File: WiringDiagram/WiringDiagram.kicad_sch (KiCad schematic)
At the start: 30 parts, among them J1 Conn_01x06, J2 Conn_01x02, J3 Conn_01x04, J4 Conn_01x04, J5 Conn_01x06, J8 FTDI SERIAL, SW1 TELEMETRUM ROTARY SWITCH, SW2 ERS SENDER ROTARY SWITCH

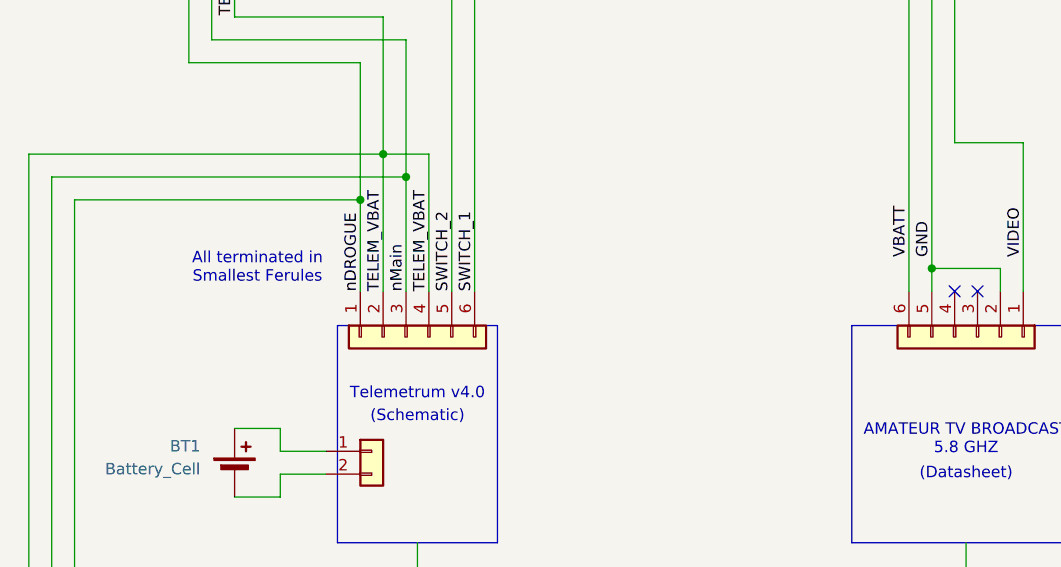
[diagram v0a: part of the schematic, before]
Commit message: Added connector notes
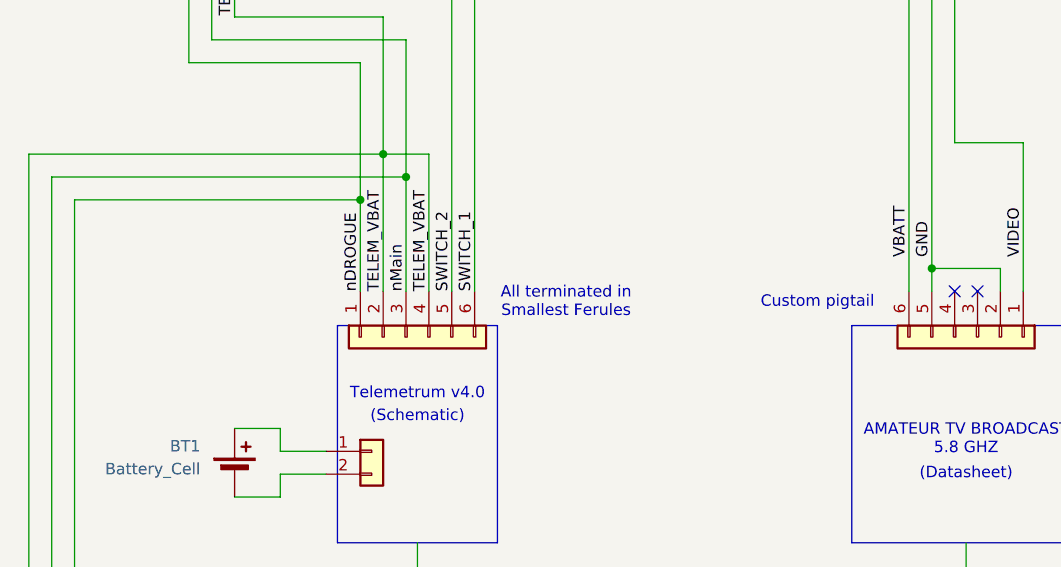
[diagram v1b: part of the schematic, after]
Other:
- note added: "Custom pigtail"
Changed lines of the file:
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@@
+		)
+	)
+	(text "Custom pigtail"
+		(exclude_from_sim no)
+		(at 242.57 118.11 0)
+		(effects
+			(font
+				(size 1.27 1.27)
+			)
 		)
 	)
@@
 	(text "All terminated in\nSmallest Ferules"
 		(exclude_from_sim no)
-		(at 180.34 114.3 0)
+		(at 214.63 118.11 0)
 		(effects
 			(font

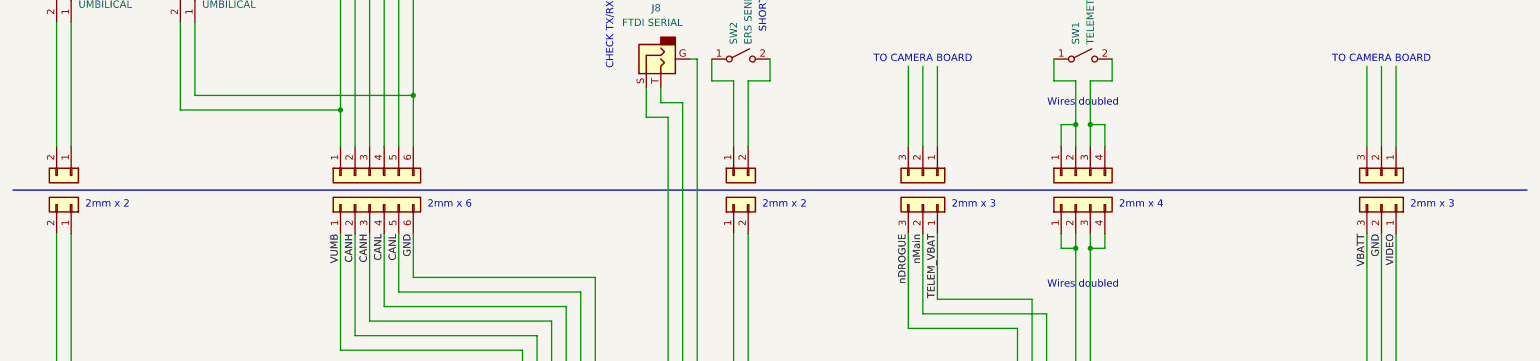
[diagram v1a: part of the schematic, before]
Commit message: Add note on extra wire length
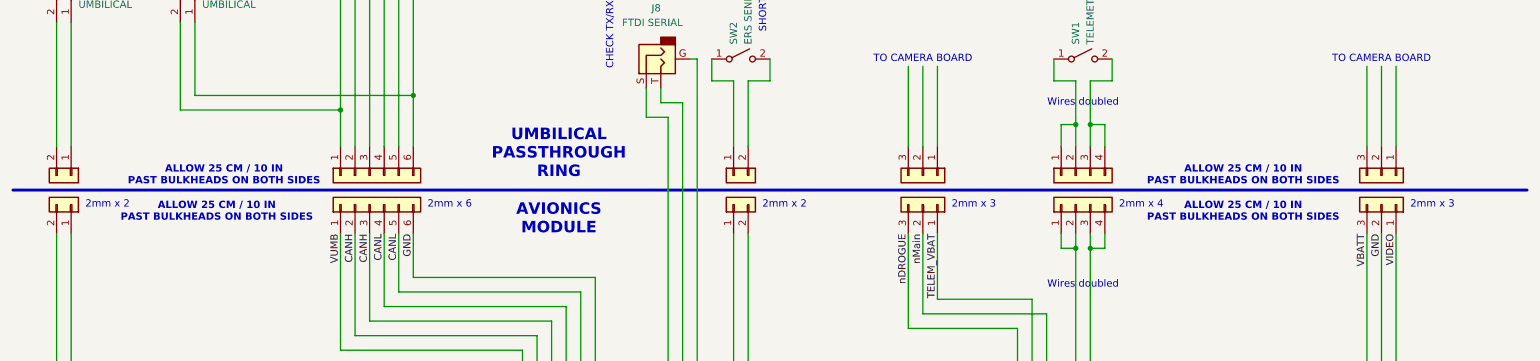
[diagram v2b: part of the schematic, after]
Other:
- note added: "ALLOW 25 CM / 10 IN PAST BULKHEADS ON BOTH SIDES"
- note added: "AVIONICS MODULE"
- note added: "UMBILICAL PASSTHROUGH RING"
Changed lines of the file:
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@@
+		)
+	)
+	(text "AVIONICS\nMODULE"
+		(exclude_from_sim no)
+		(at 111.76 72.39 0)
+		(effects
+			(font
+				(size 2 2)
+				(thickness 0.4)
+				(bold yes)
+			)
 		)
 	)
@@
 		)
 	)
+	(text "ALLOW 25 CM / 10 IN\nPAST BULKHEADS ON BOTH SIDES\n"
+		(exclude_from_sim no)
+		(at 53.34 64.77 0)
+		(effects
+			(font
+				(size 1.27 1.27)
+				(thickness 0.254)
+				(bold yes)
+			)
+		)
+	)
+	(text "UMBILICAL\nPASSTHROUGH\nRING"
+		(exclude_from_sim no)
+		(at 111.76 60.96 0)
+		(effects
+			(font
+				(size 2 2)
+				(thickness 0.4)
+				(bold yes)
+			)
+		)
+	)
 	(text "2mm x 3"
 		(exclude_from_sim no)
@@
 		)
 	)
+	(text "ALLOW 25 CM / 10 IN\nPAST BULKHEADS ON BOTH SIDES\n"
+		(exclude_from_sim no)
+		(at 231.14 64.77 0)
+		(effects
+			(font
+				(size 1.27 1.27)
+				(thickness 0.254)
+				(bold yes)
+			)
+		)
+	)
+	(text "ALLOW 25 CM / 10 IN\nPAST BULKHEADS ON BOTH SIDES\n"
+		(exclude_from_sim no)
+		(at 52.07 71.12 0)
+		(effects
+			(font
+				(size 1.27 1.27)
+				(thickness 0.254)
+				(bold yes)
+			)
+		)
+	)
 	(text "Wires doubled"
 		(exclude_from_sim no)
@@
 			(font
 				(size 1.27 1.27)
+			)
+		)
+	)
+	(text "ALLOW 25 CM / 10 IN\nPAST BULKHEADS ON BOTH SIDES\n"
+		(exclude_from_sim no)
+		(at 231.14 71.12 0)
+		(effects
+			(font
+				(size 1.27 1.27)
+				(thickness 0.254)
+				(bold yes)
 			)
 		)
@@
 		)
 		(stroke
-			(width 0)
-			(type default)
-		)
-	)
+			(width 0.508)
+			(type solid)
+		)
+	)

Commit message: Added umbilical ring connections
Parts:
- removed J-UMBILICAL, J-UMBILICAL1: UMBILICAL, symbol Connector:Conn_01x02_Socket
- added CAM-B1: 4S1P 2500?? mAh, symbol Device:Battery
- added CAM-J11, CAM-J9: BATTERY, symbol Connector_Generic:Conn_01x06
- added CAM-JP1, CAM-JP2: ~, symbol Connector_Generic:Conn_01x03
- added CAM-JP10: ATV TX, symbol Connector_Generic:Conn_01x03
- added CAM-JP12, CAM-JP13: CAMERA, symbol Connector_Generic:Conn_01x03
- added CAM-JP8: Thermistor, symbol Connector_Generic:Conn_01x02
- added ERS-J16, ERS-J17, ERS-J19, ERS-J20, ERS-J21, ERS-J22, ERS-J23: SERIAL, symbol Connector_Generic:Conn_01x03
- added ERS-J18, ERS-J24: UMB + CAN, symbol Connector_Generic:Conn_01x06
- added ERS-J26, ERS-J27, ERS-J28, ERS-J29: RocketReady, symbol Connector_Generic:Conn_01x02
- added J6: Conn_01x08, symbol Connector_Generic:Conn_01x08
- added SW3: CAMERA BOARD ROTARY SWITCH, symbol Switch:SW_SPST
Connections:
- net VBATT is gone; now on net 5V: ERS-J14.3 (Pin_3), J5.6 (Pin_6)
- net GND: now also ERS-J1.2 (Pin_2), ERS-J12.1 (Pin_1), ERS-J15.2 (Pin_2), ERS-J5.2 (Pin_2), ERS-J7.6 (Pin_6), CAM-JP10.2 (Pin_2), CAM-JP8.2 (Pin_2), ERS-J16.3 (Pin_3), ERS-J17.3 (Pin_3), ERS-J18.6 (Pin_6), ERS-J28.2 (Pin_2), ERS-J29.2 (Pin_2), J6.4 (Pin_4), J6.8 (Pin_8)
- net TELEM_VBAT: now also ERS-J13.1 (Pin_1), CAM-J9.1 (Pin_1)
- net UC_RX: now also ERS-J16.1 (Pin_1), ERS-J17.1 (Pin_1)
- net UC_TX: now also ERS-J16.2 (Pin_2), ERS-J17.2 (Pin_2)
- net VIDEO: now also ERS-J15.1 (Pin_1), CAM-JP10.3 (Pin_3)
- net VUMB: now also ERS-J7.1 (Pin_1), CAM-J9.4 (Pin_4), ERS-J18.1 (Pin_1), ERS-J28.1 (Pin_1), ERS-J29.1 (Pin_1), J6.1 (Pin_1)
- net nDROGUE: now also ERS-J13.3 (Pin_3), CAM-J9.3 (Pin_3)
- net nMain: now also ERS-J13.2 (Pin_2), CAM-J9.2 (Pin_2)
- net RR: now reaches ERS-J5.1 (Pin_1)
- net RR: now also ERS-J1.1 (Pin_1), ERS-J12.2 (Pin_2), J6.5 (Pin_5)
- net 5V: now reaches ERS-J15.3 (Pin_3)
- net 5V: now also CAM-JP10.1 (Pin_1)
- net at ERS-J7.2 (Pin_2): now also ERS-J18.2 (Pin_2)
- net at ERS-J7.3 (Pin_3): now also ERS-J18.3 (Pin_3)
- net at ERS-J7.4 (Pin_4): now also ERS-J18.4 (Pin_4)
- net at ERS-J7.5 (Pin_5): now also ERS-J18.5 (Pin_5)
- new net: ERS-J26.1 (Pin_1), SW3.1 (A)
- new net: ERS-J26.2 (Pin_2), SW3.2 (B)
- new net: CAM-B1.1 (+), CAM-J11.1 (Pin_1), CAM-J11.2 (Pin_2), CAM-J11.3 (Pin_3)
- new net: CAM-B1.2 (-), CAM-J11.4 (Pin_4), CAM-J11.5 (Pin_5), CAM-J11.6 (Pin_6)
- new net ARM+: CAM-J9.5 (Pin_5), ERS-J27.1 (Pin_1)
- new net ARM-: CAM-J9.6 (Pin_6), ERS-J27.2 (Pin_2)
- no-connect marks 2 -> 3
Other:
- note added: "CAMERA"
- note added: "Camera Board"
- note added: "LEFT OF "FRONT" SWITCH PLATE"
- note added: "MAIN ERS"
- note added: "ODU PKG.M0.8S.LG"
- note added: "REAR SWITCH PLATE"
- note added: "SWITCH CLOSED = ON"
- note added: "Switch closed = Off"
- note added: "TO CAMERA FACING DOWN?"
- note added: "TO CAMERA FACING UP?"
- note added: "TO VIDEO TX"
- note added: "UMBILICAL RING"
- note removed: "SHORTED = ON"
- note removed: "SHORTED = Off"
- note removed: "UMBILICAL PASSTHROUGH RING"
- moved on the sheet: AE1, AE2, BT1, BT2, ERS-J10, ERS-J11, ERS-J12, ERS-J3, ERS-J5, ERS-J8, J8, SW1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

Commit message: Minor polishing
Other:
- note added: "GND connection for VUMB :("
- note added: "TO FRONT CAMERA FACING DOWN"
- note added: "TO FRONT CAMERA FACING UP"
- note removed: "TO CAMERA FACING DOWN?"
- note removed: "TO CAMERA FACING UP?"
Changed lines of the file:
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@@
 		)
 	)
-	(text "TO CAMERA FACING DOWN?"
-		(exclude_from_sim no)
-		(at 454.66 289.56 0)
+	(text "TO FRONT CAMERA \nFACING DOWN"
+		(exclude_from_sim no)
+		(at 450.85 289.56 0)
 		(effects
 			(font
@@
 		)
 	)
+	(text "GND connection\nfor VUMB :("
+		(exclude_from_sim no)
+		(at 388.62 300.99 90)
+		(effects
+			(font
+				(size 1.27 1.27)
+			)
+			(justify left)
+		)
+	)
 	(text "Telemetrum v4.0"
 		(exclude_from_sim no)
@@
 		)
 	)
-	(text "TO CAMERA FACING UP?"
-		(exclude_from_sim no)
-		(at 453.39 314.96 0)
-		(effects
-			(font
+	(text "TO FRONT CAMERA \nFACING UP"
+		(exclude_from_sim no)
+		(at 452.12 314.96 0)
+		(effects
+			(font

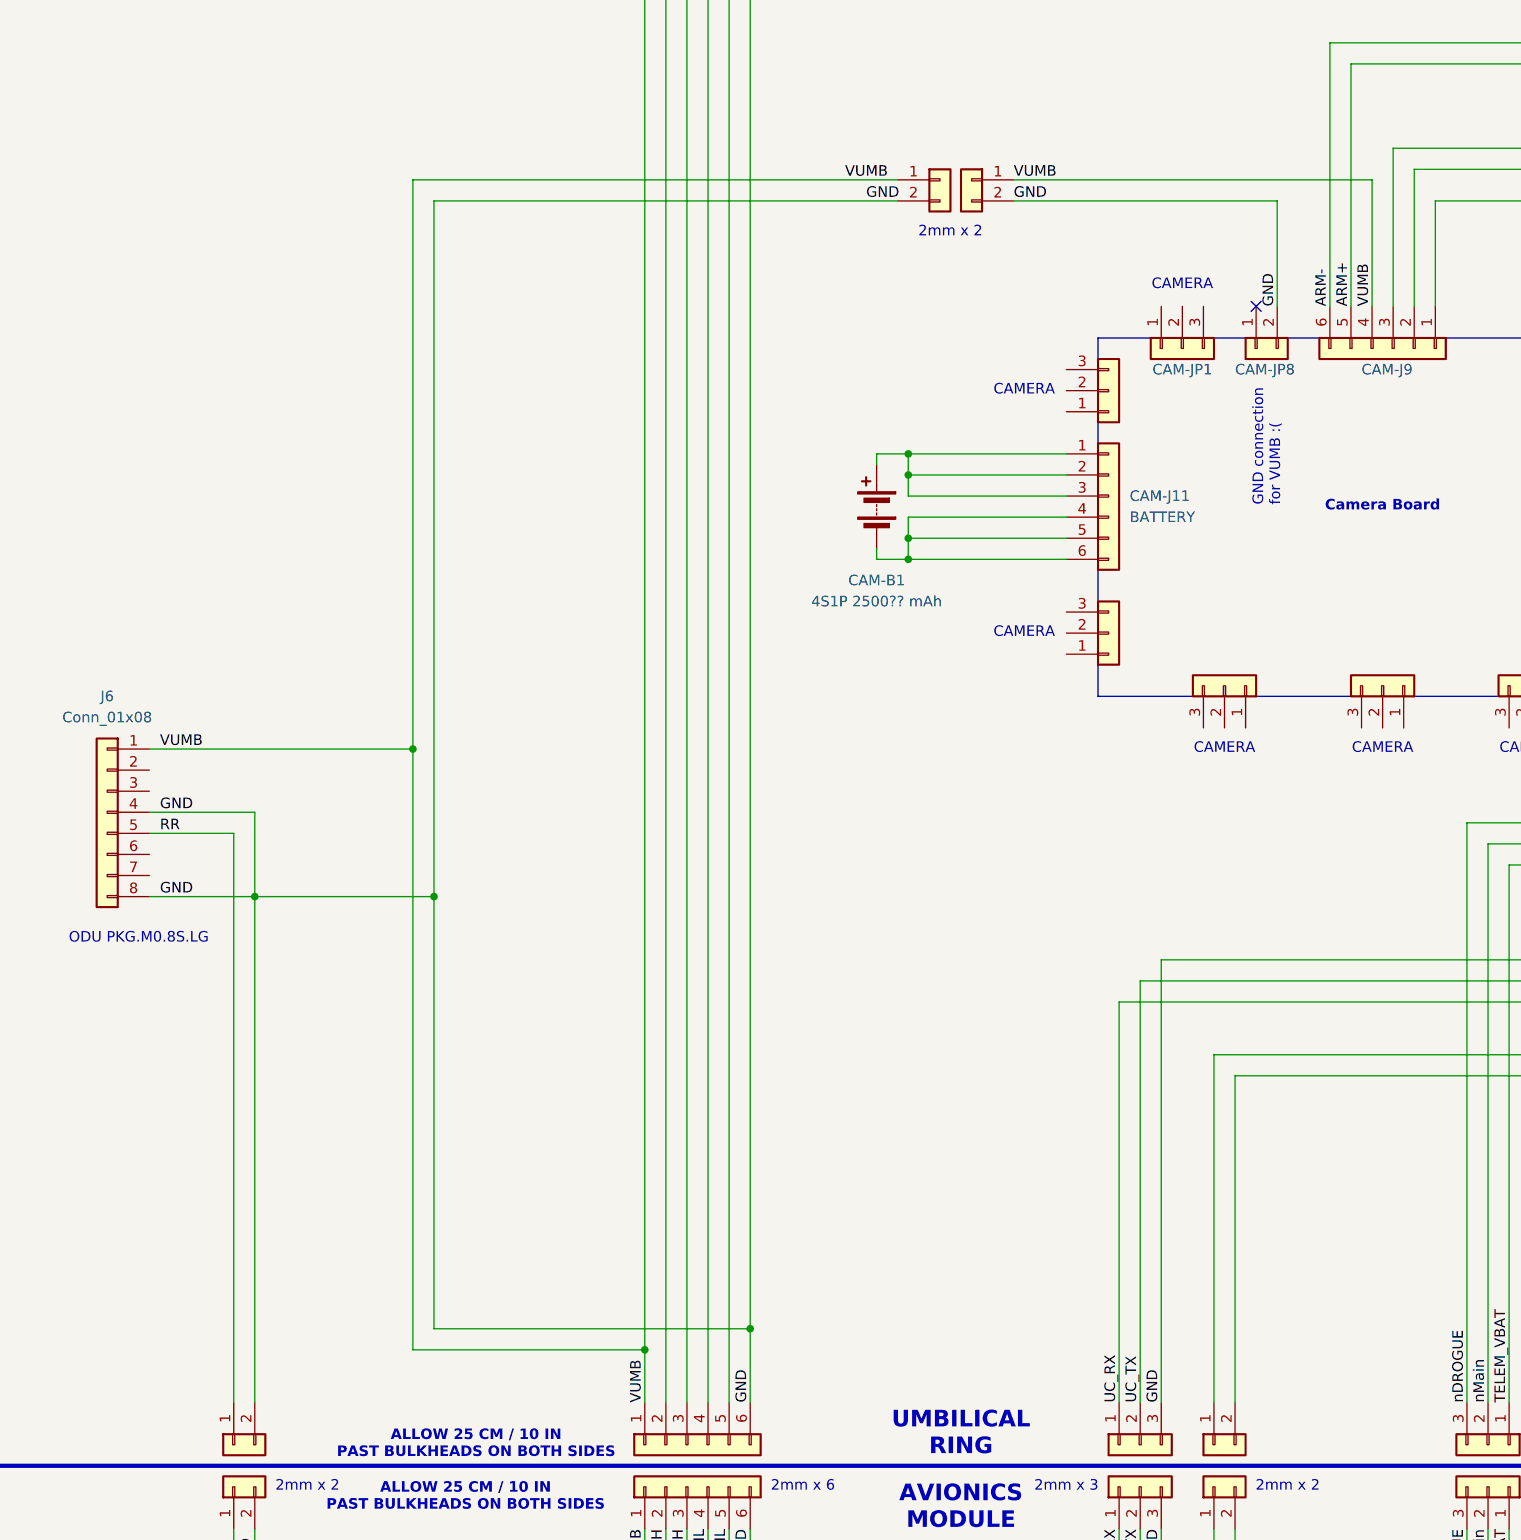
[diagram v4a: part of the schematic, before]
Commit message: Added another connector on umbilical cord
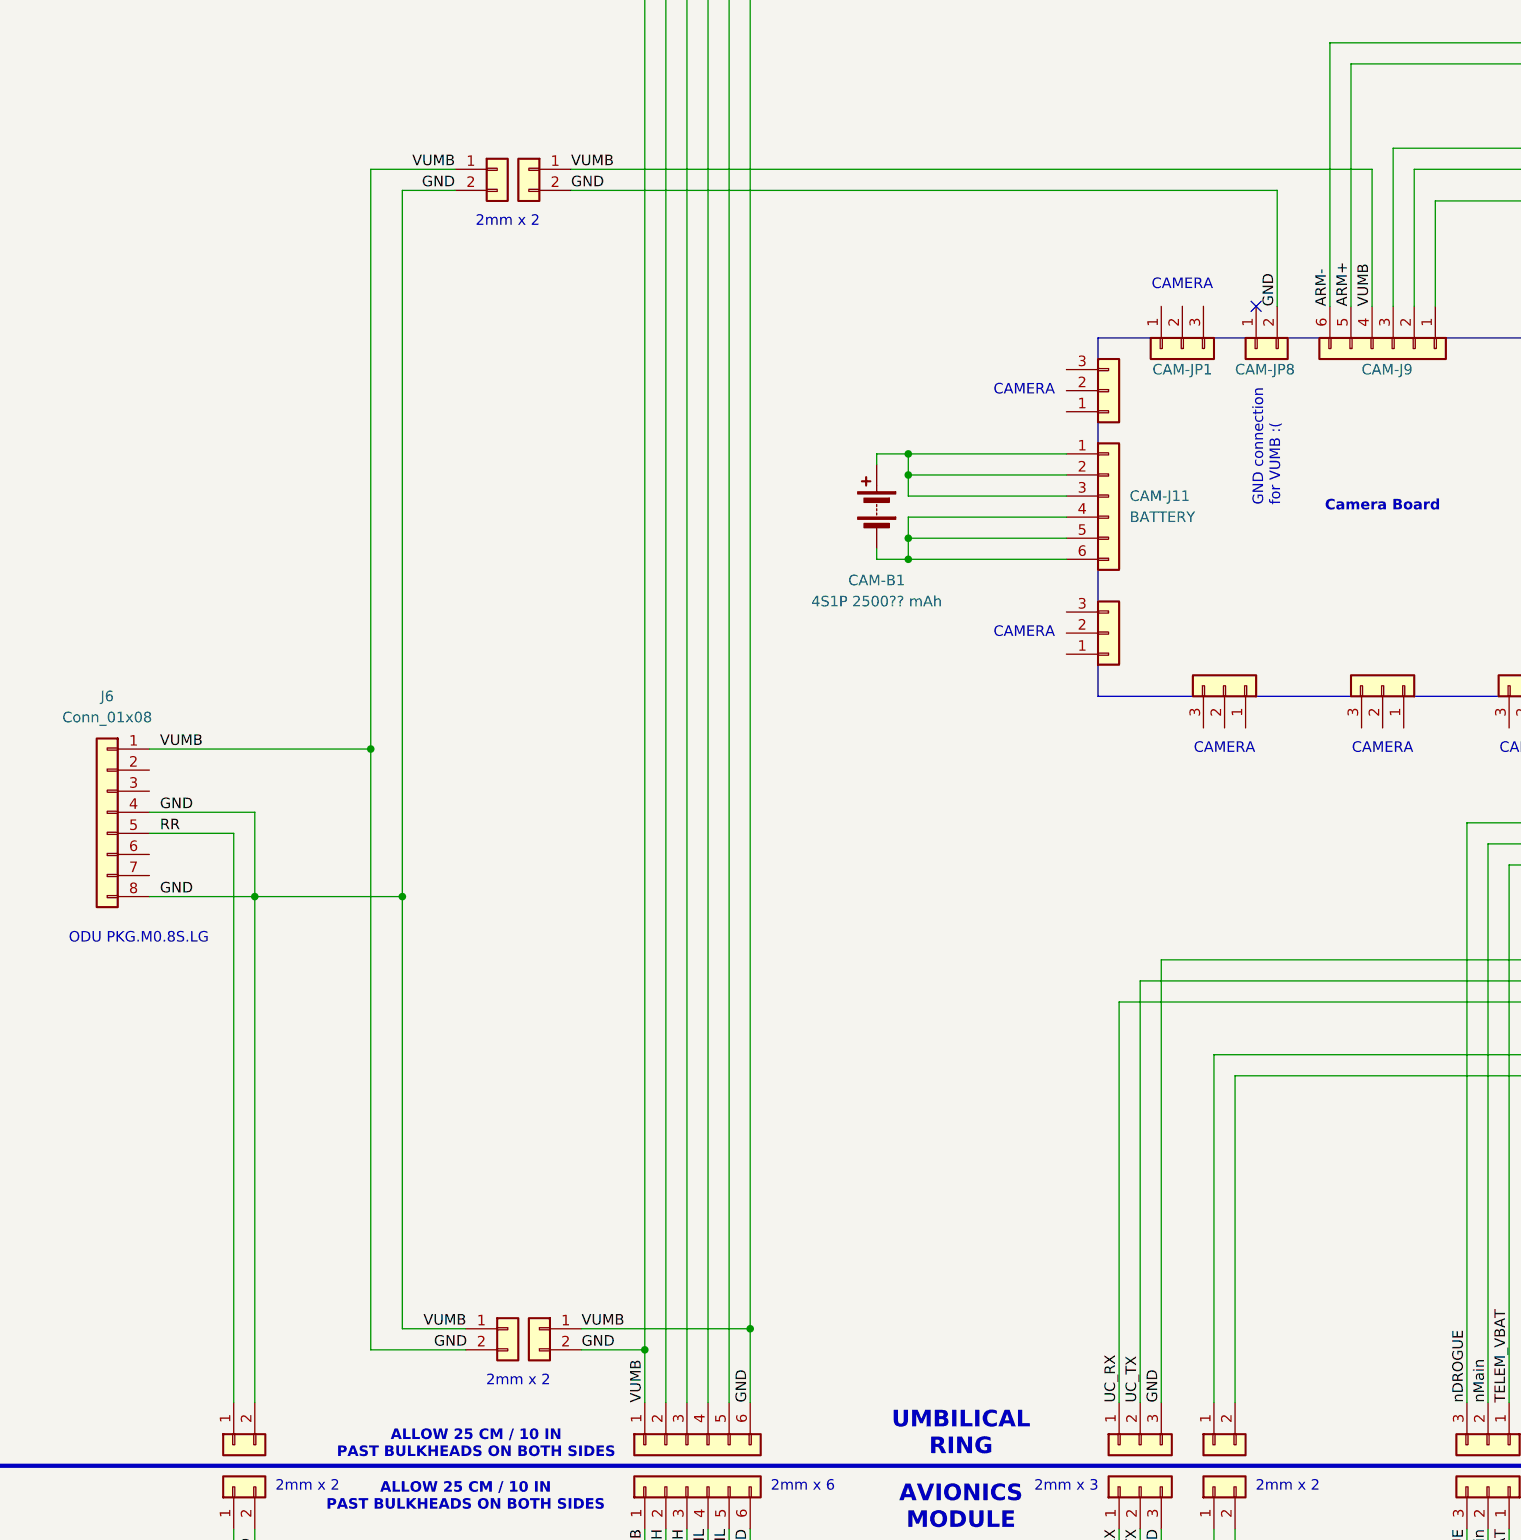
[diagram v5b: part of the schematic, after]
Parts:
- added ERS-J25, ERS-J30: RocketReady, symbol Connector_Generic:Conn_01x02
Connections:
- net VUMB is gone; now on net GND: CAM-J9.4 (Pin_4), ERS-J18.1 (Pin_1), ERS-J28.1 (Pin_1), ERS-J29.1 (Pin_1), ERS-J6.1 (Pin_1), ERS-J7.1 (Pin_1), ERS-J8.1 (Pin_1), J6.1 (Pin_1)
- net GND: now also ERS-J25.1 (Pin_1), ERS-J25.2 (Pin_2), ERS-J30.1 (Pin_1), ERS-J30.2 (Pin_2)
